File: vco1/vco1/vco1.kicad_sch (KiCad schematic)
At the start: 33 parts, among them J1 Conn_02x08_Odd_Even, J2 AudioJack2_SwitchT, J3 AudioJack2_SwitchT, J4 AudioJack2_SwitchT, J5 AudioJack2_SwitchT, J6 AudioJack2_SwitchT, J7 AudioJack2_SwitchT, J8 AudioJack2_SwitchT, J9 AudioJack2_SwitchT, SW1 SW_SPDT, U1 SSI2131, U2 TL431DBZ, U3 TL074

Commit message: Draw some more stuff
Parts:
- added C10, C8: 10n, Capacitor_SMD:C_0603_1608Metric_Pad1.08x0.95mm_HandSolder, symbol Device:C
- added C11, C12: 100n, Capacitor_SMD:C_0603_1608Metric_Pad1.08x0.95mm_HandSolder, symbol Device:C
- added C9: 1u, Capacitor_SMD:C_0603_1608Metric_Pad1.08x0.95mm_HandSolder, symbol Device:C
- added FB1, FB2, FB3: FerriteBead_Small, Inductor_SMD:L_1206_3216Metric_Pad1.22x1.90mm_HandSolder, symbol Device:FerriteBead_Small
- added Q1: BC847, Package_TO_SOT_SMD:SOT-23, symbol Transistor_BJT:BC847
- added R10: 270, Resistor_SMD:R_0603_1608Metric_Pad0.98x0.95mm_HandSolder, symbol Device:R
- added R11: 267k, Resistor_SMD:R_0603_1608Metric_Pad0.98x0.95mm_HandSolder, symbol Device:R
- added R12: 4k3, Resistor_SMD:R_0603_1608Metric_Pad0.98x0.95mm_HandSolder, symbol Device:R
- added R13: 22k1, Resistor_SMD:R_0603_1608Metric_Pad0.98x0.95mm_HandSolder, symbol Device:R
- added R14, R15, R17: 49k9, Resistor_SMD:R_0603_1608Metric_Pad0.98x0.95mm_HandSolder, symbol Device:R
- added R16: 1M maybe?, Resistor_SMD:R_0603_1608Metric_Pad0.98x0.95mm_HandSolder, symbol Device:R
- added R18, R19: 100k, Resistor_SMD:R_0603_1608Metric_Pad0.98x0.95mm_HandSolder, symbol Device:R
- added R20, R21: 499k, Resistor_SMD:R_0603_1608Metric_Pad0.98x0.95mm_HandSolder, symbol Device:R
- added R22, R6, R7: 10k, Resistor_SMD:R_0603_1608Metric_Pad0.98x0.95mm_HandSolder, symbol Device:R
- added R23: 20k, Resistor_SMD:R_0603_1608Metric_Pad0.98x0.95mm_HandSolder, symbol Device:R
- added R24: 47k5, Resistor_SMD:R_0603_1608Metric_Pad0.98x0.95mm_HandSolder, symbol Device:R
- added R25: 3k3, Resistor_SMD:R_0603_1608Metric_Pad0.98x0.95mm_HandSolder, symbol Device:R
- added R26: 1k maybe, Resistor_SMD:R_0603_1608Metric_Pad0.98x0.95mm_HandSolder, symbol Device:R
- added R27: 1k maybe?, Resistor_SMD:R_0603_1608Metric_Pad0.98x0.95mm_HandSolder, symbol Device:R
- added R4, R5: 39k, Resistor_SMD:R_0603_1608Metric_Pad0.98x0.95mm_HandSolder, symbol Device:R
- added R8, R9: 1k, Resistor_SMD:R_0603_1608Metric_Pad0.98x0.95mm_HandSolder, symbol Device:R
- added RV_CALIB1: 5k 10 turn, Potentiometer_THT:Potentiometer_Bourns_3266Y_Vertical, symbol Device:R_Potentiometer
- added unit 5 of U3
- C1, C4, C5, C6: footprint (none) -> Capacitor_SMD:C_0603_1608Metric_Pad1.08x0.95mm_HandSolder
- C2, C3: footprint (none) -> Capacitor_THT:CP_Radial_D5.0mm_P2.50mm
- C7: value 4.7u -> 4.7u or so; footprint (none) -> Capacitor_SMD:C_0805_2012Metric_Pad1.18x1.45mm_HandSolder
- D1, D2: footprint (none) -> LED_SMD:LED_0603_1608Metric_Pad1.05x0.95mm_HandSolder
- J1: footprint (none) -> Connector_IDC:IDC-Header_2x08_P2.54mm_Vertical
- J_CV1: renamed from J2; footprint (none) -> Connector_Audio:Jack_3.5mm_QingPu_WQP-PJ398SM_Vertical_CircularHoles
- J_CV2: renamed from J3; footprint (none) -> Connector_Audio:Jack_3.5mm_QingPu_WQP-PJ398SM_Vertical_CircularHoles
- J_FM1: renamed from J4; footprint (none) -> Connector_Audio:Jack_3.5mm_QingPu_WQP-PJ398SM_Vertical_CircularHoles
- J_PULSE1: renamed from J8; footprint (none) -> Connector_Audio:Jack_3.5mm_QingPu_WQP-PJ398SM_Vertical_CircularHoles
- J_PWM1: renamed from J5; footprint (none) -> Connector_Audio:Jack_3.5mm_QingPu_WQP-PJ398SM_Vertical_CircularHoles
- J_SAW1: renamed from J7; footprint (none) -> Connector_Audio:Jack_3.5mm_QingPu_WQP-PJ398SM_Vertical_CircularHoles
- J_SYNC1: renamed from J6; footprint (none) -> Connector_Audio:Jack_3.5mm_QingPu_WQP-PJ398SM_Vertical_CircularHoles
- J_TRI1: renamed from J9; footprint (none) -> Connector_Audio:Jack_3.5mm_QingPu_WQP-PJ398SM_Vertical_CircularHoles
- R1, R2, R3: footprint (none) -> Resistor_SMD:R_0603_1608Metric_Pad0.98x0.95mm_HandSolder
- RV_CV2: renamed from RV1; value R_Potentiometer -> 100k?; footprint (none) -> Potentiometer_THT:Potentiometer_Alpha_RD901F-40-00D_Single_Vertical_CircularHoles
- RV_PWM1: renamed from RV4; value R_Potentiometer -> 100k; footprint (none) -> Potentiometer_THT:Potentiometer_Alpha_RD901F-40-00D_Single_Vertical_CircularHoles
- RV_RANGE1: renamed from RV2; value R_Potentiometer -> 100k; footprint (none) -> Potentiometer_THT:Potentiometer_Alpha_RD901F-40-00D_Single_Vertical_CircularHoles
- RV_TUNE1: renamed from RV3; value R_Potentiometer -> 100k; footprint (none) -> Potentiometer_THT:Potentiometer_Alpha_RD901F-40-00D_Single_Vertical_CircularHoles
- SW1: footprint (none) -> Button_Switch_THT:SW_Slide_SPDT_Straight_CK_OS102011MS2Q
- U1: footprint Package_SO:SOP-16_3.9x9.9mm_P1.27mm -> Package_SO:STC_SOP-16_3.9x9.9mm_P1.27mm
- U3: footprint (none) -> Package_SO:SOIC-14_3.9x8.7mm_P1.27mm
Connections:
- net +12V: now also RV_RANGE1.1, RV_TUNE1.1, C11.1, FB2.2, U3.4 (V+); no longer J1.10 (Pin_10), J1.9 (Pin_9)
- net +2V5: now also C1.1, RV_PWM1.1, U2.1 (K), U2.2 (REF), R13.1, R20.1, R25.1
- net +5V: now also FB3.2, Q1.3 (C), R23.1, R25.2; no longer J1.11 (Pin_11), J1.12 (Pin_12)
- net -12V: now also C12.2, FB1.2, R24.2, U3.11 (V-); no longer J1.1 (Pin_1), J1.2 (Pin_2)
- net 1.25V: now also U3.10 (+), U3.5 (+)
- net GND: now also C1.2, J_CV1.S, J_CV1.TN, J_CV2.S, J_FM1.S, J_PULSE1.S, J_PWM1.S, J_SAW1.S, J_SYNC1.S, J_TRI1.S, RV_CV2.1, RV_PWM1.3, RV_RANGE1.3, RV_TUNE1.3, SW1.2 (B), U2.3 (A), C11.2, C12.1, C8.2, R12.2, R19.1, R22.2, R26.2, R27.2; no longer U3.12 (+)
- net PULSE_OUT: now also R6.2
- net TCAP: now also C7.1
- net TRI_OUT: now also R7.2
- net at J_PWM1.T: now also R18.1
- net at J_CV1.T: now also R14.1
- net at J_TRI1.T: now also R9.1
- net at U3.14: now also D2.2 (A)
- net at U3.6 (-): now also R4.2, R6.1
- net at U3.7: now also R4.1, R8.2
- net at SW1.1 (A): now also C7.2
- net at RV_TUNE1.2: now also R16.1
- net HARD_SYNC: now reaches U1.10 (HARD_SYNC)
- net HARD_SYNC: now also D1.2 (A), C10.2, Q1.2 (E), R22.1
- net LIN_FREQ: now reaches U1.12 (LIN_FREQ)
- net LIN_FREQ: now also R20.2, R21.2
- net at U1.13 (EXPO_SCALE): now also RV_CALIB1.1
- net BW_COMP: now reaches U1.15 (BW_COMP)
- net BW_COMP: now also R10.1
- net PWM_CTRL: now reaches U1.3 (PWM_CTRL)
- net PWM_CTRL: now also RV_PWM1.2, R18.2, R19.2
- net HF_TRACK: now reaches U1.5 (HF_TRACK)
- net HF_TRACK: now also R11.1, R12.1
- net EXPO_FREQ: now reaches U1.6 (EXPO_FREQ)
- net EXPO_FREQ: now also R11.2, R14.2, R15.2, R16.2, R17.2
- net at J_CV2.T: now also RV_CV2.3
- net at J_SYNC1.T: now also C10.1
- net at D1.1 (K): now also R27.1
- net at J_FM1.T: now also C9.1
- net at RV_CV2.2: now also R15.1
- net at RV_RANGE1.2: now also R17.1
- net at J_PULSE1.T: now also R8.1
- net at U3.8: now also R5.1, R9.2
- net at U3.9 (-): now also U3.12 (+), R5.2, R7.1
- net at D2.1 (K): now also R26.1
- new net: FB3.1, J1.11 (Pin_11), J1.12 (Pin_12)
- new net: R13.2, RV_CALIB1.2, RV_CALIB1.3
- new net: Q1.1 (B), R23.2, R24.1
- new net: C9.2, R21.1
- new net: C8.1, R10.2
- new net: FB1.1, J1.1 (Pin_1), J1.2 (Pin_2)
- new net: FB2.1, J1.10 (Pin_10), J1.9 (Pin_9)
- no-connect marks 0 -> 3
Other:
- note added: "20µA per octave"
- note added: "Anti-hangup app note AB503"
- note added: "Do the math here, this is wrong. Maybe opamp buffer inputs?"
- note added: "Shift from 1.25Vpp centred at 1.25V to 5Vpp centred at 0V"
- note removed: "Noise gen"
- note removed: "Shift from 1.25Vpp centred at 1.25V 5Vpp centred at 0V"
- note removed: "Why -1.25V ref to opamp? Why not just put ½VREF on + input? Or just capacitively couple it."
- moved on the sheet: C1, C4, C5, C6, C7, D1, D2, J_CV1, J_CV2, J_FM1, J_PULSE1, J_PWM1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

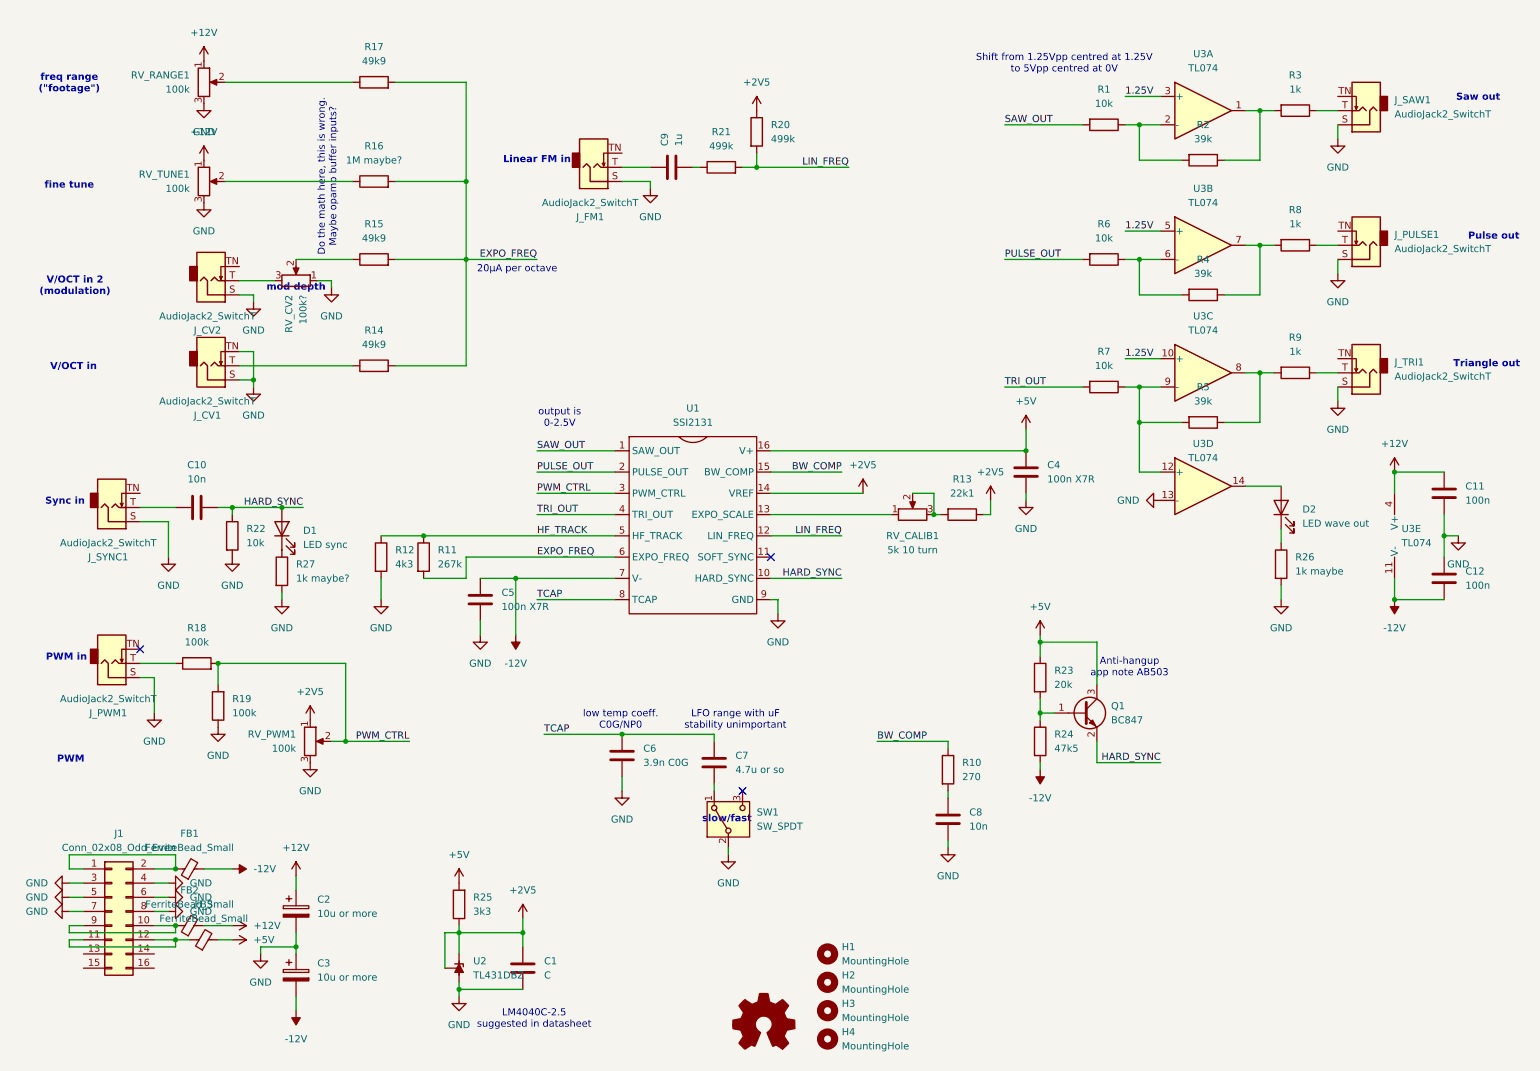
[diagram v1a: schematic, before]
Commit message: Route most of the board
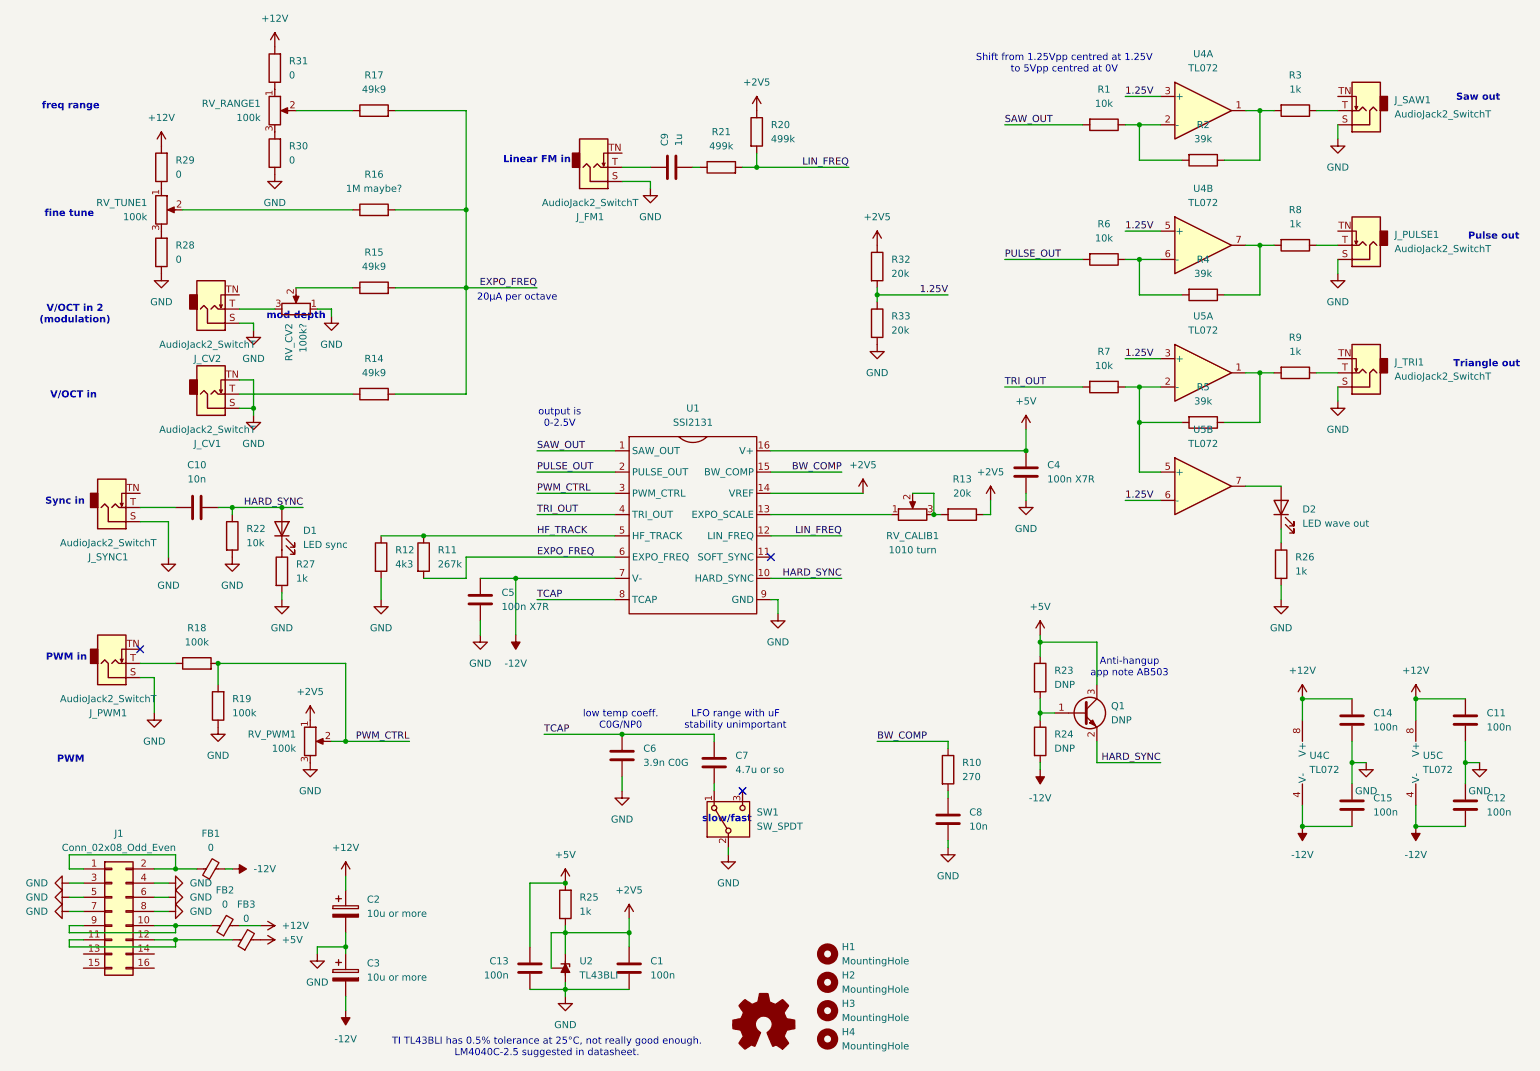
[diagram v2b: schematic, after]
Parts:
- removed U3: TL074, symbol Amplifier_Operational:TL074
- added C13, C14, C15: 100n, Capacitor_SMD:C_0603_1608Metric_Pad1.08x0.95mm_HandSolder, symbol Device:C
- added R28, R29, R30, R31: 0, Resistor_SMD:R_0603_1608Metric_Pad0.98x0.95mm_HandSolder, symbol Device:R
- added R32, R33: 20k, Resistor_SMD:R_0603_1608Metric_Pad0.98x0.95mm_HandSolder, symbol Device:R
- added U4, U5: TL072, Package_SO:SOIC-8_3.9x4.9mm_P1.27mm, symbol Amplifier_Operational:TL072
- C1: value C -> 100n
- D1, D2: footprint LED_SMD:LED_0603_1608Metric_Pad1.05x0.95mm_HandSolder -> LED_THT:LED_D3.0mm
- FB1, FB2, FB3: value FerriteBead_Small -> 0
- Q1: value BC847 -> DNP
- R13: value 22k1 -> 20k
- R23: value 20k -> DNP
- R24: value 47k5 -> DNP
- R25: value 3k3 -> 1k
- R26: value 1k maybe -> 1k
- R27: value 1k maybe? -> 1k
- RV_CALIB1: value 5k 10 turn -> 1010 turn
- U2: value TL431DBZ -> TL43BLI
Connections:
- net +12V: now also C14.1, R29.2, R31.2, U4.8 (V+), U5.8 (V+); no longer RV_RANGE1.1, RV_TUNE1.1
- net +2V5: now also R32.1
- net +5V: now also C13.2
- net -12V: now also C15.2, U4.4 (V-), U5.4 (V-)
- net 1.25V: now also R32.2, R33.1, U4.3 (+), U4.5 (+), U5.3 (+), U5.6 (-)
- net GND: now also C13.1, C14.2, C15.1, R28.1, R30.1, R33.2; no longer RV_RANGE1.3, RV_TUNE1.3
- net at R2.1, R3.2: now also U4.1
- net at R1.1, R2.2: now also U4.2 (-)
- net at R4.1, R8.2: now also U4.7
- net at R4.2, R6.1: now also U4.6 (-)
- net at R5.2, R7.1: now also U5.2 (-), U5.5 (+)
- net at D2.2 (A): now also U5.7
- net at R5.1, R9.2: now also U5.1
- new net: R31.1, RV_RANGE1.1
- new net: R29.1, RV_TUNE1.1
- new net: R28.2, RV_TUNE1.3
- new net: R30.2, RV_RANGE1.3
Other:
- note added: "TI TL43BLI has 0.5% tolerance at 25°C, not really good enough. LM4040C-2.5 suggested in datasheet."
- note added: "freq range"
- note removed: "Do the math here, this is wrong. Maybe opamp buffer inputs?"
- note removed: "LM4040C-2.5 suggested in datasheet"
- note removed: "freq range ("footage")"
- moved on the sheet: C1, C11, C12, C2, C3, FB1, FB2, FB3, J_CV1, J_CV2, R14, R15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

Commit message: More routing and stuff
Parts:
- removed FB1, FB2, FB3: 0, Inductor_SMD:L_1206_3216Metric_Pad1.22x1.90mm_HandSolder, symbol Device:FerriteBead_Small
- C2, C3: value 10u or more -> 10u
- C7: value 4.7u or so -> 2.2u
- C9: value 1u -> 2.2u; footprint Capacitor_SMD:C_0603_1608Metric_Pad1.08x0.95mm_HandSolder -> Capacitor_SMD:C_0805_2012Metric_Pad1.18x1.45mm_HandSolder
- RV_CALIB1: value 1010 turn -> 10k 3266Y-103
- RV_CV2: value 100k? -> 100k; footprint Potentiometer_THT:Potentiometer_Alpha_RD901F-40-00D_Single_Vertical_CircularHoles -> Pot:RV9012NO
- RV_PWM1, RV_RANGE1, RV_TUNE1: footprint Potentiometer_THT:Potentiometer_Alpha_RD901F-40-00D_Single_Vertical_CircularHoles -> Pot:RV9012NO
- U2: value TL43BLI -> TL431BCDBZR
- U4, U5: value TL072 -> TL072HxD
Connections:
- net +12V: now also J1.10 (Pin_10), J1.9 (Pin_9)
- net +5V: now also J1.11 (Pin_11), J1.12 (Pin_12)
- net -12V: now also J1.1 (Pin_1), J1.2 (Pin_2)
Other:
- note added: "TI TL431Bx has 0.5% tolerance at 25°C, not really good enough. LM4040C-2.5 suggested in datasheet."
- note removed: "TI TL43BLI has 0.5% tolerance at 25°C, not really good enough. LM4040C-2.5 suggested in datasheet."

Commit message: Fix footprints, add test points
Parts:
- added TP1, TP2, TP3, TP4, TP5, TP6, TP7: TestPoint_Alt, Holes:TP_0.9mm, symbol Connector:TestPoint_Alt
- SW1: footprint Button_Switch_THT:SW_Slide_SPDT_Straight_CK_OS102011MS2Q -> Switch:SPDT big pads
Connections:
- net +2V5: now also TP3.1
- net EXPO_FREQ: now also TP2.1
- net GND: now also TP7.1
- net HF_TRACK: now also TP5.1
- net LIN_FREQ: now also TP4.1
- net TCAP: now also TP6.1
- net TRI_OUT: now also TP1.1

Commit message: VCO prototype 1 to Aisler
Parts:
- R16: value 1M maybe? -> 1M
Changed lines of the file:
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@@
 			)
 		)
-		(property "Value" "1M maybe?"
+		(property "Value" "1M"
 			(at 78.74 38.1 90)
 			(effects
